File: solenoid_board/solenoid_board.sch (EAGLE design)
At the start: 18 parts, among them Q1 MOSFET-NCHANNELSMD, Q2 MOSFET-NCHANNELSMD, Q3 MOSFET-NCHANNELSMD, Q4 MOSFET-NCHANNELSMD

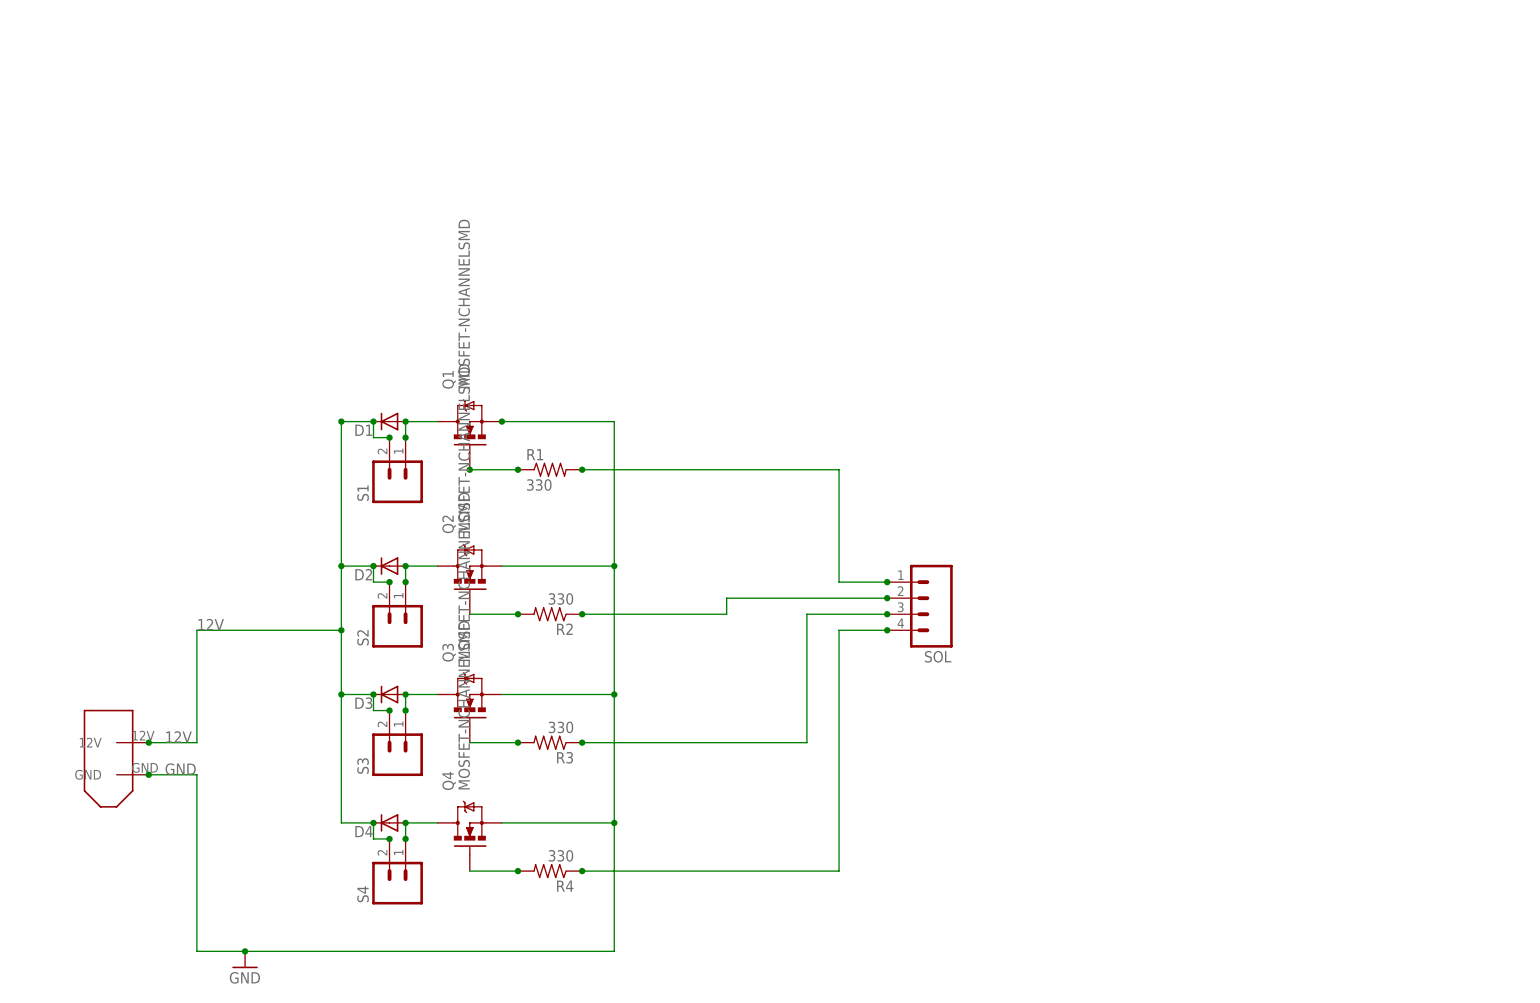
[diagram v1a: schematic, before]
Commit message: Updated Solenoid Board to Rev C
- Added 10k pull-down resistors to MOSFET gates

DFM: https://www.freedfm.com/freedfm/0019486703400185/results/summary2.htm

Change-Id: I212b2e5e4622d924b76152e8610cd9dcc6a01ff7
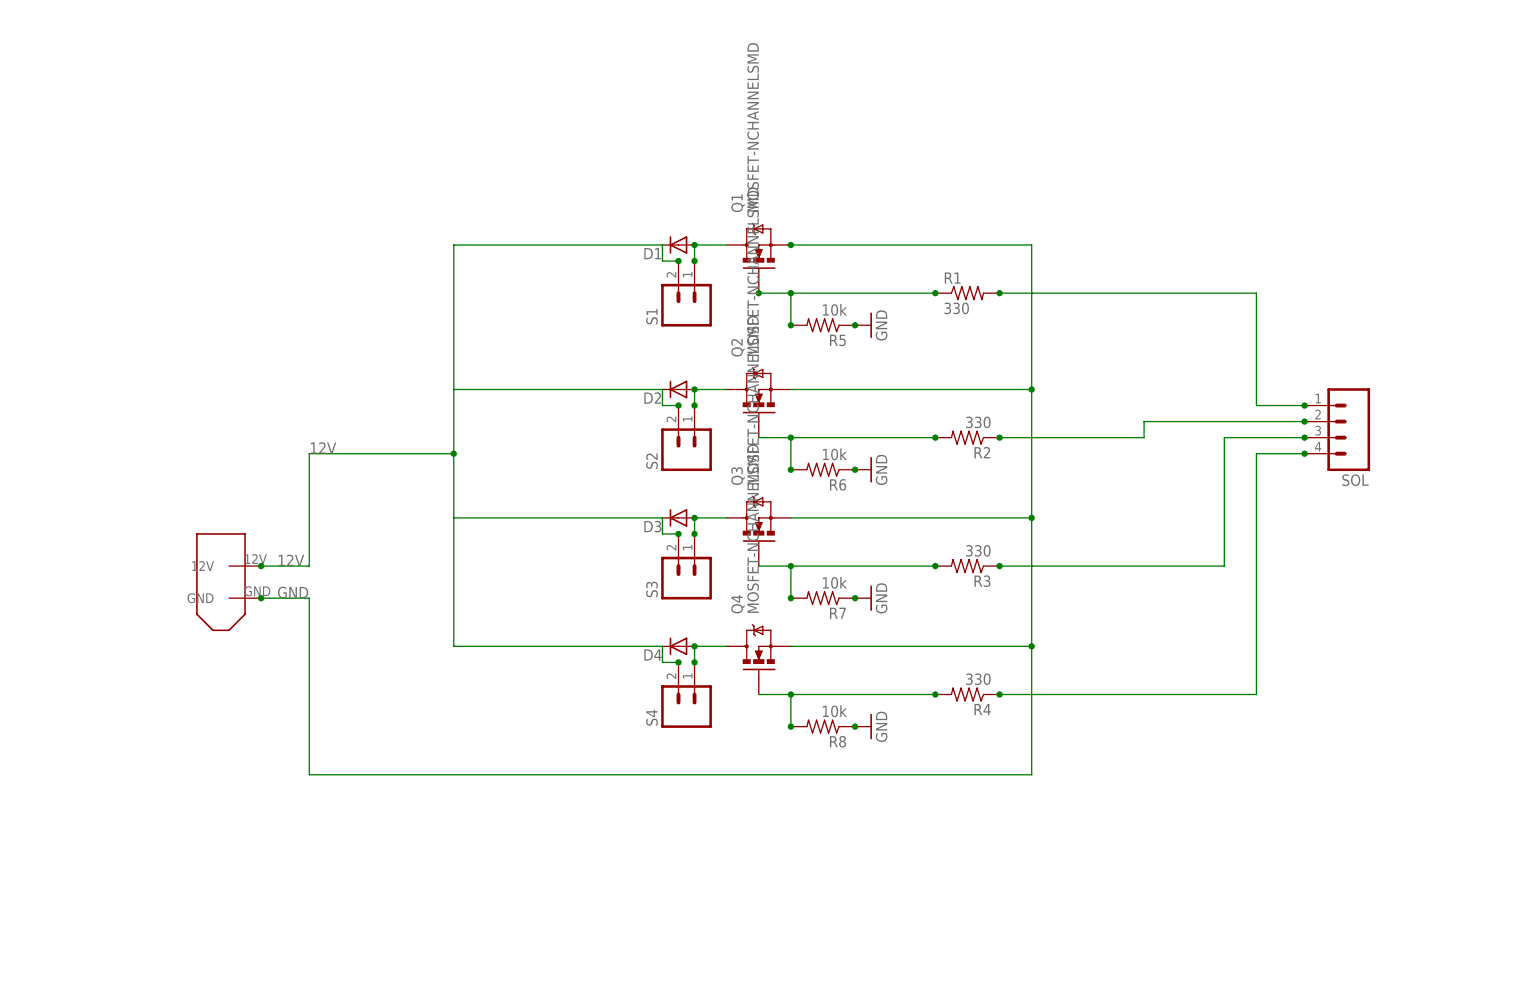
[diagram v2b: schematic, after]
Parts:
- added R5, R6, R7, R8: 10k, resistor:R-US_R0603
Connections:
- net GND: now also R5.1, R6.1, R7.1, R8.1
- net N$15: now also R5.2
- net N$16: now also R6.2
- net N$17: now also R7.2
- net N$18: now also R8.2
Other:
- moved on the sheet: D1, D2, D3, D4, Q1, Q2, Q3, Q4, R1, R2, R3, R4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

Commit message: Updated Sherlock, Watson & Solenoid Board to Rev D. Updated pie.lbr.
- Put SSOP16 footprint and symbol (from Sparkfun.lbr) in pie.lbr.
  Can be used as a template for any SSOP16 device.
- Created SSOP14 footprint and symbol in pie.lbr using SSOP16.
  Can be used as a template for any SSOP14 device.
- Added QUADNOR device to pie.lbr
- Added VCC and enable pin to solenoid connector on Watson
- Added enable pin for solenoid board on Sherlock
- Added quad-NOR gate onto Solenoid Board
- Added VCC and enable pin for quad-NOR gate on Solenoid Board
- Added 0.1uF capacitors between VCC&GND and 12V&GND for Solenoid Board
- Added mounting holes to Solenoid Board
- Added additional holes to Sherlock and Watson for the testing jig
- Replaced all holes with standoff part in pie.lbr
- Gave each hole a value, either "Mounting", "Test" or "Mounting + Test"
  to state their purpose.
- Added/copied devices on boards that were NOT in pie.lbr TO pie.lbr
- Removed unnecessary packages from copied devices
- Manually set pad diameters for through-hole packages that were
  added/created/already there for these three boards
- Added PARTNUMBER attribute to the library parts added/copied/
  created/already there for these three boards
- Moved all Sherlock passives to the top

RYAN: I fixed what you asked for this revision. If this goes
through, I will then work on fixing everything else you told me to.

Sherlock DFM: https://www.freedfm.com/freedfm/0019486703414971/results/summary2.htm
Watson DFM: https://www.freedfm.com/freedfm/0019486703414975/results/summary2.htm
Solenoid Board DFM: https://www.freedfm.com/freedfm/0019486703414973/results/summary2.htm

Change-Id: Ie6b1bdecadde8b7bc780ad23041f2e110bf24a4c
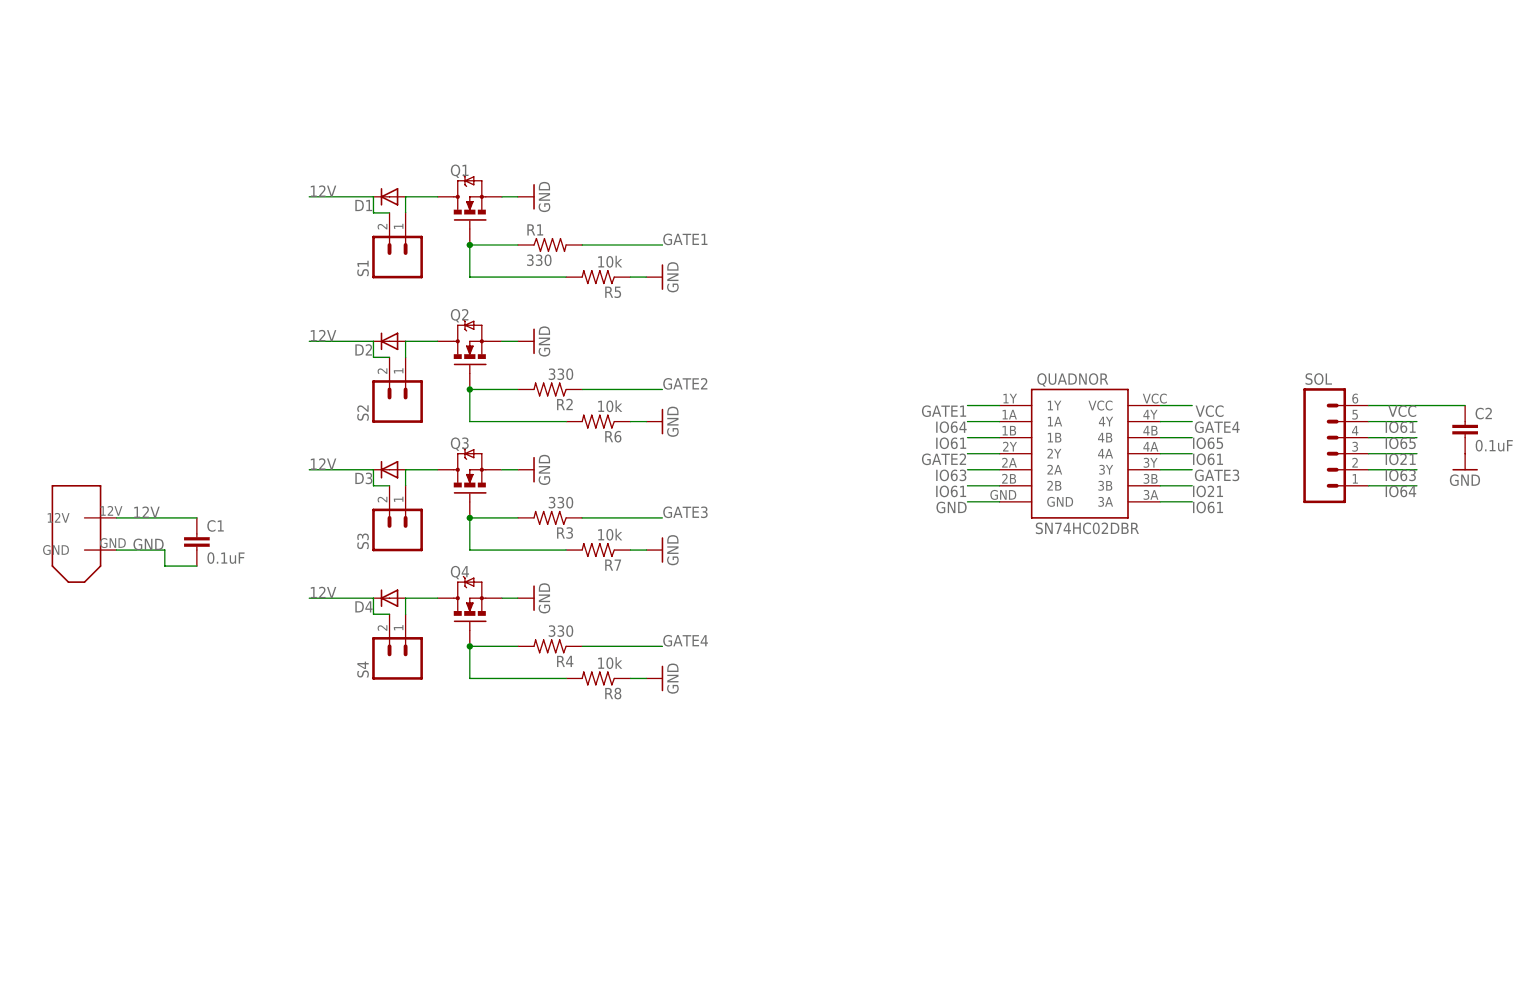
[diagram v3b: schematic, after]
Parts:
- added C1, C2: 0.1uF, pie:CAP0603-CAP
- added QUADNOR: SN74HC02DBR, pie:SN74HC02DBR
- D1, D2, D3, D4: device SparkFun:DIODESMA-ALT -> pie:DIODESMA-ALT
- Q1, Q2, Q3, Q4: device SparkFun:MOSFET-NCHANNELSMD -> pie:MOSFET-NCHANNELSMD
- R1, R2, R3, R4, R5, R6, R7, R8: device resistor:R-US_R0603 -> pie:R-US_R0603
- S1, S2, S3, S4: value M02 -> (none); device pie:M02 -> pie:M021X02-MTA
- SOL: value M04 -> M06; device pie:M04 -> pie:M06
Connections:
- removed net N$1: R1.2, SOL.1
- removed net N$5: R2.1, SOL.2
- removed net N$6: R3.1, SOL.3
- removed net N$7: R4.1, SOL.4
- new net GATE1: QUADNOR.1Y, R1.2
- new net GATE2: QUADNOR.2Y, R2.1
- new net GATE3: QUADNOR.3Y, R3.1
- new net GATE4: QUADNOR.4Y, R4.1
- new net IO21: QUADNOR.3B, SOL.3
- new net IO61: QUADNOR.1B, QUADNOR.2B, QUADNOR.3A, QUADNOR.4A, SOL.5
- new net IO63: QUADNOR.2A, SOL.2
- new net IO64: QUADNOR.1A, SOL.1
- new net IO65: QUADNOR.4B, SOL.4
- new net VCC: C2.1, QUADNOR.VCC, SOL.6
- net 12V: now also C1.1
- net GND: now also C1.2, C2.2, QUADNOR.GND
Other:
- moved on the sheet: D1, D2, D3, D4, Q1, Q2, Q3, Q4, R1, R2, R3, R4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

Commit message: Sherlock, Watson, and Solenoid Rev E
- Updated all parts on all boards with their new
  versions in pie.lbr
- Cleaned up silkscreens and made names more
  meaningful
- Cleaned up schematics

This is intended to be the final version for all
three boards. There will be one more revision,
but that is only to add the copyright info Ryan
is making for the schematics and boards.

A side-effect of cleaning up the schematics is
that some connections may have been severd and
traces may have disappeared. I've tried my best
to detect and re-route those traces. If you find
any, please let me know. Thanks.

Sherlock DFM: https://www.freedfm.com/freedfm/0019486703422743/results/summary2.htm
Watson DFM: https://www.freedfm.com/freedfm/0019486703422746/results/summary2.htm
Solenoid DFM: https://www.freedfm.com/freedfm/0019486703422817/results/summary2.htm

Change-Id: I0ddac82c4f4e303a663db72d1e0729480dfd451e
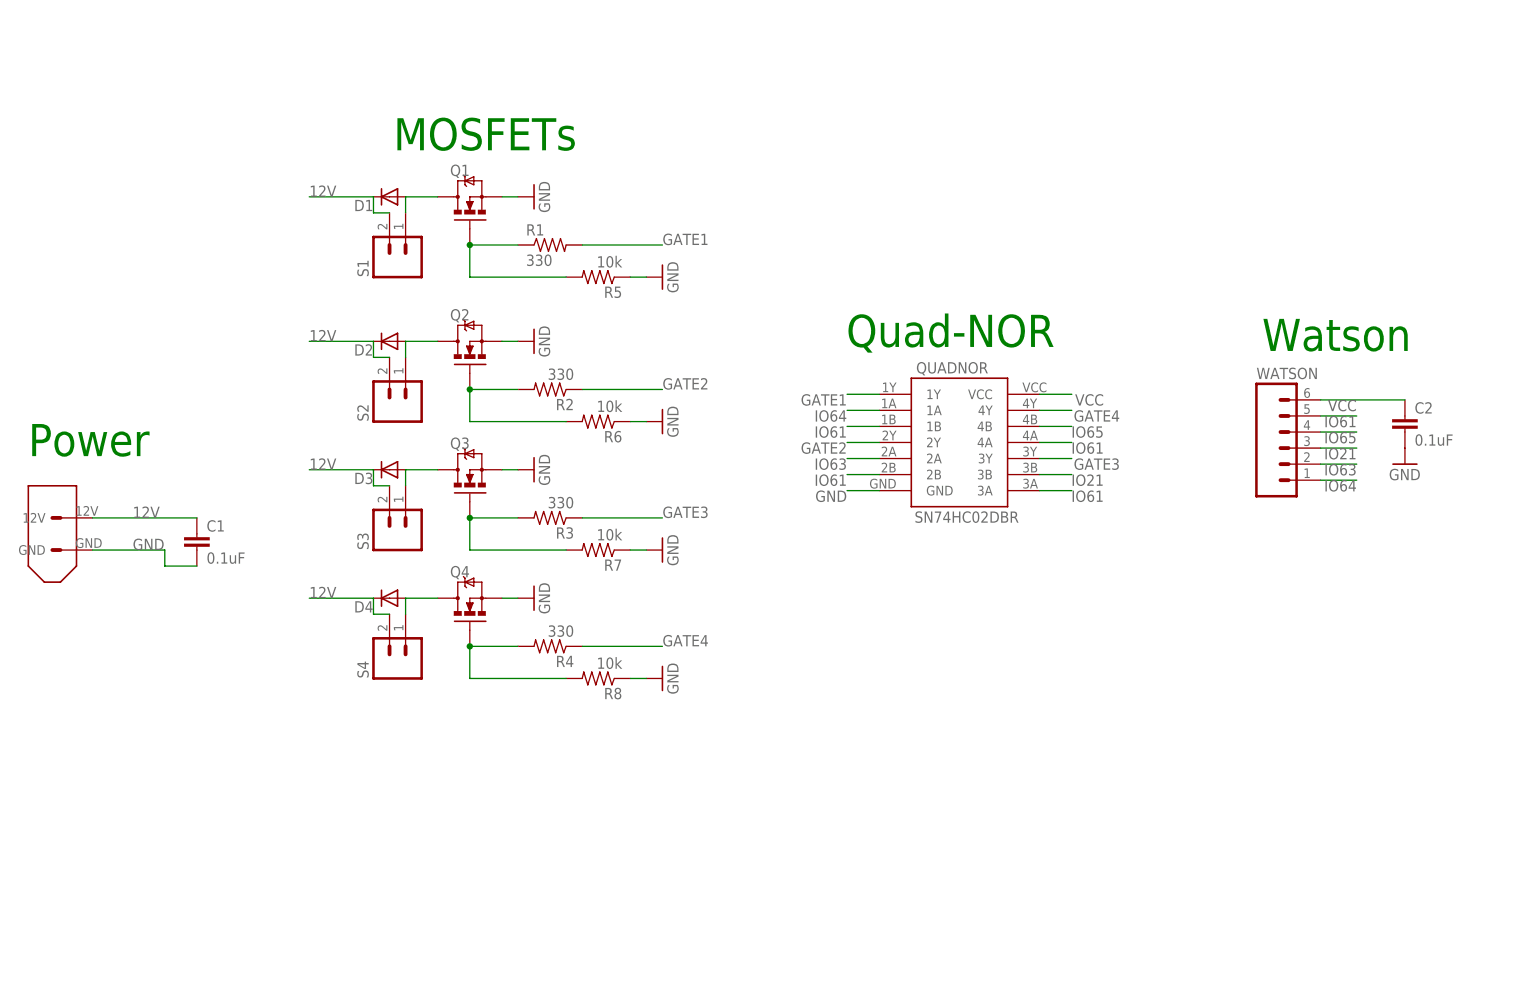
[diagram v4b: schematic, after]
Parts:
- removed SOL: M06, pie:M06
- added WATSON: M06, pie:M06
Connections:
- net IO21: now also WATSON.3; no longer SOL.3
- net IO61: now also WATSON.5; no longer SOL.5
- net IO63: now also WATSON.2; no longer SOL.2
- net IO64: now also WATSON.1; no longer SOL.1
- net IO65: now also WATSON.4; no longer SOL.4
- net VCC: now also WATSON.6; no longer SOL.6
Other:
- note added: "MOSFETs"
- note added: "Power"
- note added: "Quad-NOR"
- note added: "Watson"
- moved on the sheet: C2, QUADNOR

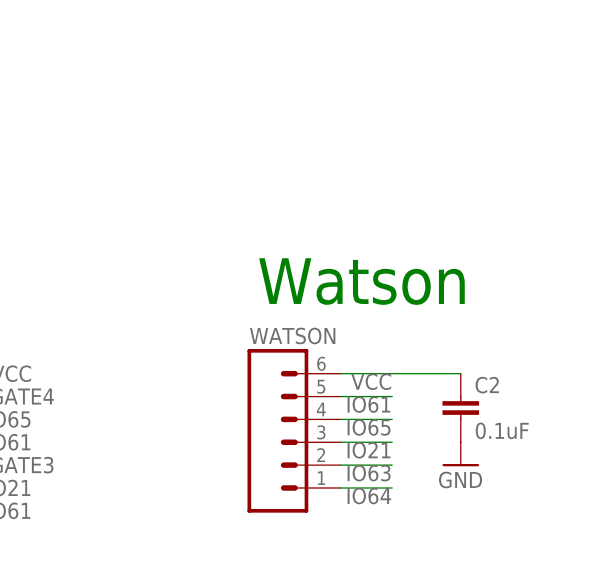
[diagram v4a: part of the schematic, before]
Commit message: Sherlock/Watson/Solenoid Rev E (Again)
Had to make a few simple changes Dennis requested.
This is the final version. Rev F will only contain
extra copyright material.

Sherlcok DFM: https://www.freedfm.com/freedfm/0019486703424644/results/summary2.htm
Watson DFM: https://www.freedfm.com/freedfm/0019486703424641/results/summary2.htm
Solenoid DFM: https://www.freedfm.com/freedfm/0019486703424640/results/summary2.htm

Change-Id: Ibaa3e17f4a8e9033ce9bcff25cf747d321aea476
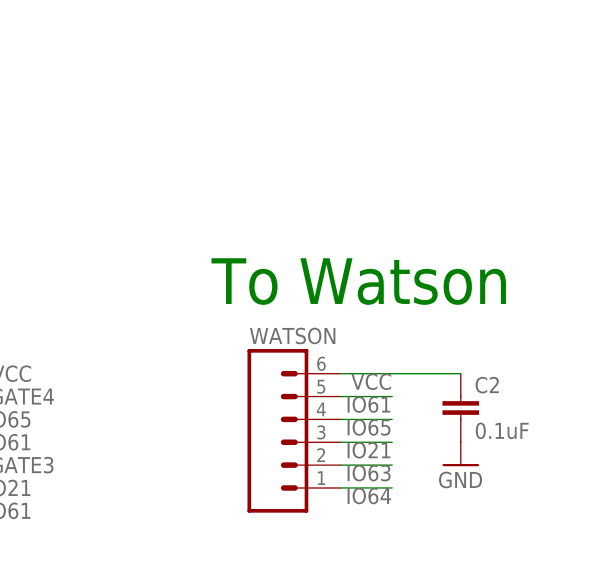
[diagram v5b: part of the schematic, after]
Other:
- note added: "To Watson"
- note removed: "Watson"
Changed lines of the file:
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@@
 <text x="8.89" y="106.299" size="5.08" layer="91">Power</text>
 <text x="138.303" y="123.571" size="5.08" layer="91">Quad-NOR</text>
-<text x="204.089" y="122.936" size="5.08" layer="91">Watson</text>
+<text x="199.009" y="122.936" size="5.08" layer="91">To Watson</text>
 <text x="66.675" y="154.686" size="5.08" layer="91">MOSFETs</text>
 </plain>
